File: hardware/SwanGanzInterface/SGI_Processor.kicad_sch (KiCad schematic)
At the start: 15 parts, among them J5 Conn_01x08_Pin, U7 LP-MSPM0G3507, U8 Adafruit ST7735R, U9 FT232R

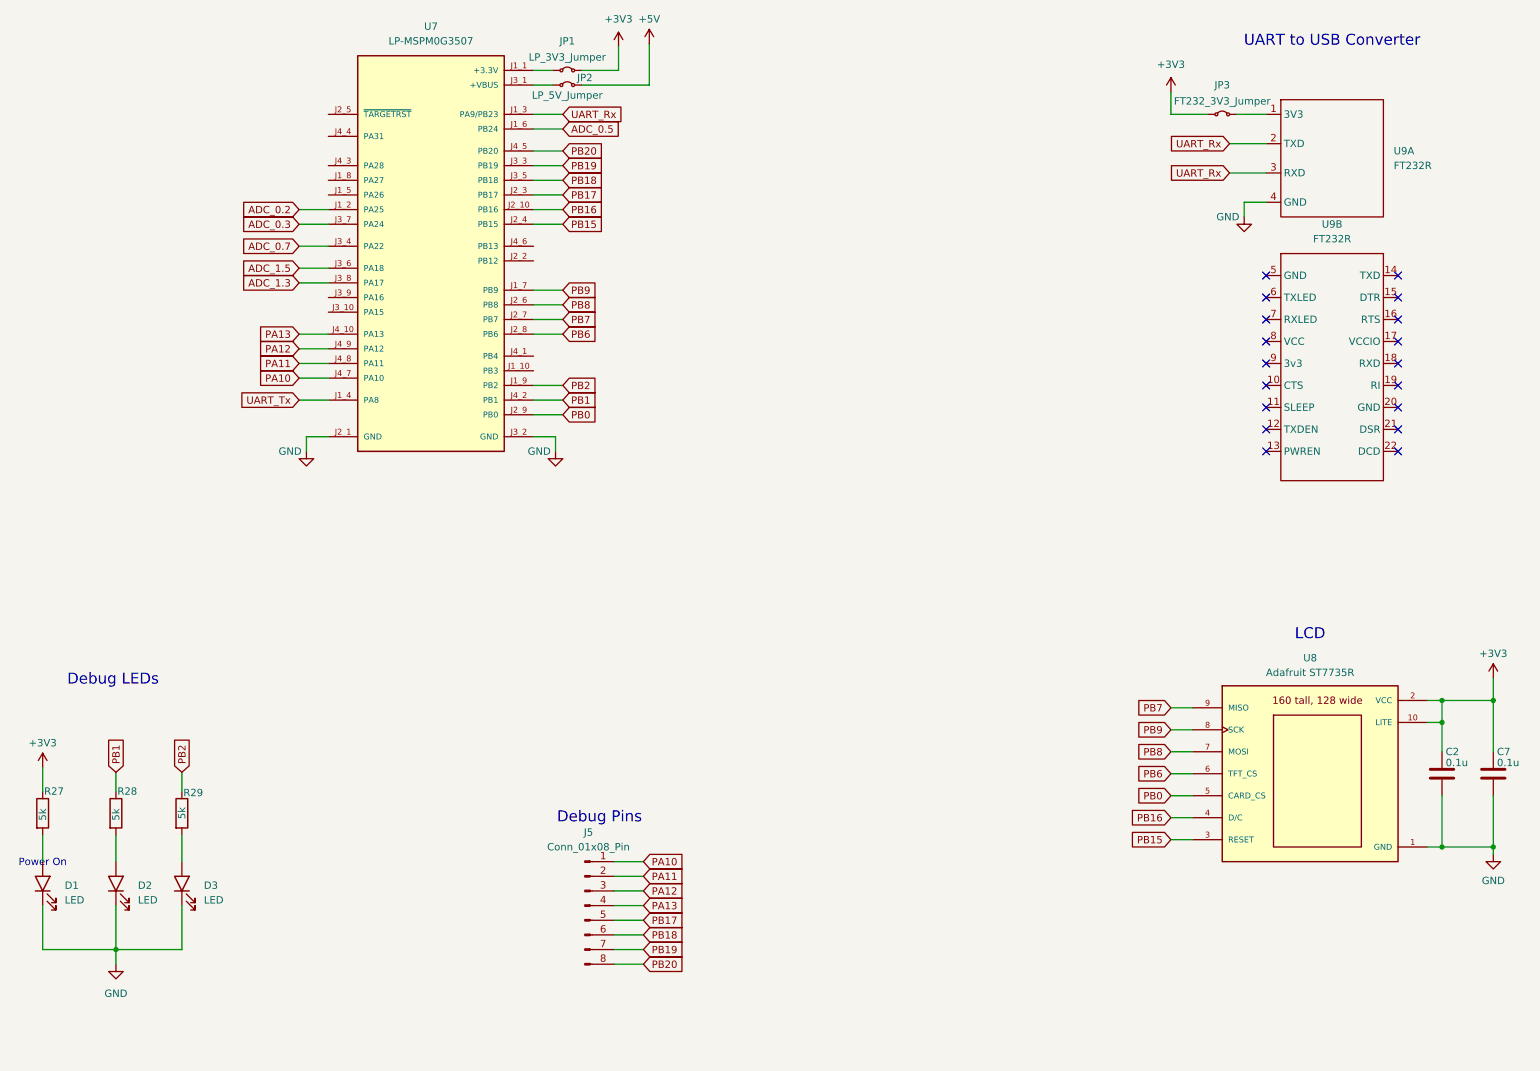
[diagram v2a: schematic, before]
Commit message: Added Test Points to the Outputs of Analog Circuits
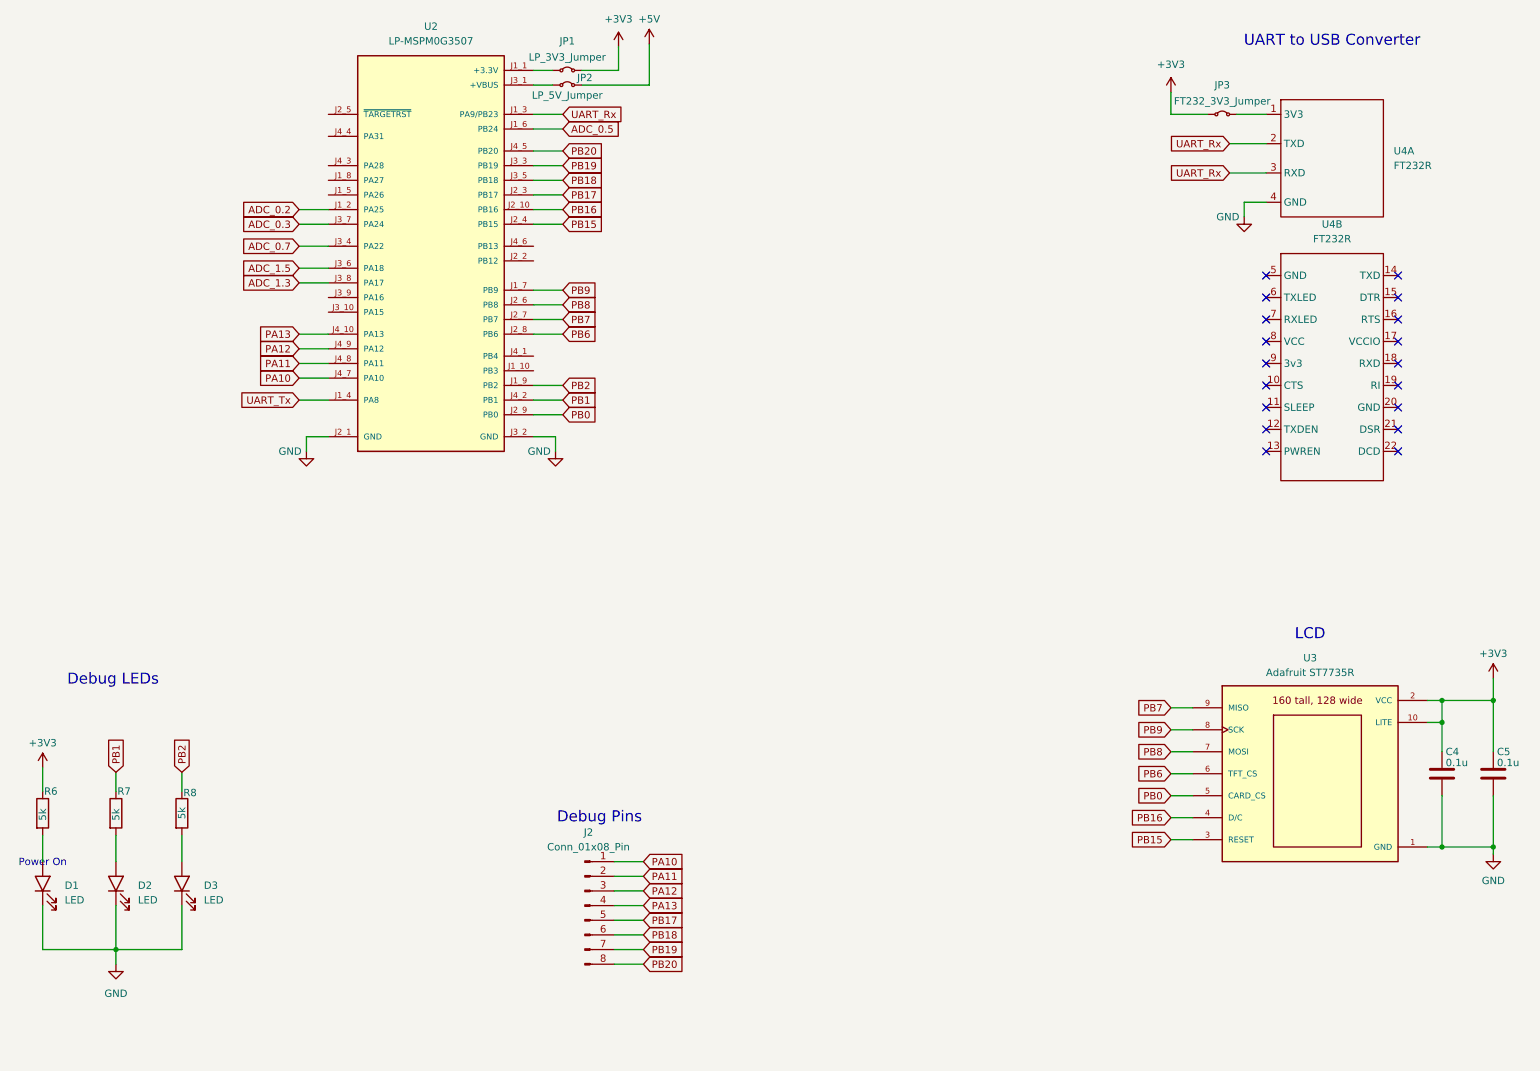
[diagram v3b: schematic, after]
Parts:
- C4: renamed from C2; footprint (none) -> Capacitor_SMD:C_0603_1608Metric
- C5: renamed from C7; footprint (none) -> Capacitor_SMD:C_0603_1608Metric
- renumbered J5 to J2, R27 to R6, R28 to R7, R29 to R8, U7 to U2, U8 to U3, U9 to U4
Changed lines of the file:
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@@
 		(on_board yes)
 		(dnp no)
-		(property "Reference" "#PWR058"
+		(property "Reference" "#PWR023"
 			(at 116.84 96.52 0)
 			(effects
@@
 			(project "SwanGanzInterface"
 				(path "/4e9a6e30-f660-472b-9696-bea1f34b4545/b7986f9d-7bcd-462e-9f66-fb6deb5be406"
-					(reference "#PWR058")
+					(reference "#PWR023")
 					(unit 1)
 				)
@@
 		(on_board yes)
 		(dnp no)
-		(property "Reference" "R27"
+		(property "Reference" "R6"
 			(at 28.194 149.098 0)
 			(effects
@@
 			(project ""
 				(path "/4e9a6e30-f660-472b-9696-bea1f34b4545/b7986f9d-7bcd-462e-9f66-fb6deb5be406"
-					(reference "R27")
+					(reference "R6")
 					(unit 1)
 				)
@@
 		(on_board yes)
 		(dnp no)
-		(property "Reference" "#PWR057"
+		(property "Reference" "#PWR022"
 			(at 73.66 96.52 0)
 			(effects
@@
 			(project "SwanGanzInterface"
 				(path "/4e9a6e30-f660-472b-9696-bea1f34b4545/b7986f9d-7bcd-462e-9f66-fb6deb5be406"
-					(reference "#PWR057")
+					(reference "#PWR022")
 					(unit 1)
 				)
@@
 		(dnp no)
 		(fields_autoplaced yes)
-		(property "Reference" "#PWR045"
+		(property "Reference" "#PWR029"
 			(at 279.4 166.37 0)
 			(effects
@@
 			(project ""
 				(path "/4e9a6e30-f660-472b-9696-bea1f34b4545/b7986f9d-7bcd-462e-9f66-fb6deb5be406"
-					(reference "#PWR045")
+					(reference "#PWR029")
 					(unit 1)
 				)
@@
 		(dnp no)
 		(fields_autoplaced yes)
-		(property "Reference" "J5"
+		(property "Reference" "J2"
 			(at 122.555 156.21 0)
 			(effects
@@
 			(project ""
 				(path "/4e9a6e30-f660-472b-9696-bea1f34b4545/b7986f9d-7bcd-462e-9f66-fb6deb5be406"
-					(reference "J5")
+					(reference "J2")
 					(unit 1)
 				)
@@
 		(dnp no)
 		(fields_autoplaced yes)
-		(property "Reference" "U9"
+		(property "Reference" "U4"
 			(at 251.46 50.8 0)
 			(effects
@@
 			(project ""
 				(path "/4e9a6e30-f660-472b-9696-bea1f34b4545/b7986f9d-7bcd-462e-9f66-fb6deb5be406"
-					(reference "U9")
+					(reference "U4")
 					(unit 2)
 				)
@@
 		(dnp no)
 		(fields_autoplaced yes)
-		(property "Reference" "#PWR049"
+		(property "Reference" "#PWR028"
 			(at 279.4 133.35 0)
 			(effects
@@
 			(project ""
 				(path "/4e9a6e30-f660-472b-9696-bea1f34b4545/b7986f9d-7bcd-462e-9f66-fb6deb5be406"
-					(reference "#PWR049")
+					(reference "#PWR028")
 					(unit 1)
 				)
@@
 		(dnp no)
 		(fields_autoplaced yes)
-		(property "Reference" "#PWR060"
+		(property "Reference" "#PWR025"
 			(at 133.096 23.368 0)
 			(effects
@@
 			(project ""
 				(path "/4e9a6e30-f660-472b-9696-bea1f34b4545/b7986f9d-7bcd-462e-9f66-fb6deb5be406"
-					(reference "#PWR060")
+					(reference "#PWR025")
 					(unit 1)
 				)
@@
 		(on_board yes)
 		(dnp no)
-		(property "Reference" "R29"
+		(property "Reference" "R8"
 			(at 52.324 149.352 0)
 			(effects
@@
 			(project "SwanGanzInterface"
 				(path "/4e9a6e30-f660-472b-9696-bea1f34b4545/b7986f9d-7bcd-462e-9f66-fb6deb5be406"
-					(reference "R29")
+					(reference "R8")
 					(unit 1)
 				)
@@
 		(dnp no)
 		(fields_autoplaced yes)
-		(property "Reference" "U9"
+		(property "Reference" "U4"
 			(at 262.128 38.0999 0)
 			(effects
@@
 			(project ""
 				(path "/4e9a6e30-f660-472b-9696-bea1f34b4545/b7986f9d-7bcd-462e-9f66-fb6deb5be406"
-					(reference "U9")
+					(reference "U4")
 					(unit 1)
 				)
@@
 		(dnp no)
 		(fields_autoplaced yes)
-		(property "Reference" "U8"
+		(property "Reference" "U3"
 			(at 247.65 125.984 0)
 			(effects
@@
 			(project ""
 				(path "/4e9a6e30-f660-472b-9696-bea1f34b4545/b7986f9d-7bcd-462e-9f66-fb6deb5be406"
-					(reference "U8")
+					(reference "U3")
 					(unit 1)
 				)
@@
 		(on_board yes)
 		(dnp no)
-		(property "Reference" "C7"
+		(property "Reference" "C5"
 			(at 280.035 142.24 0)
 			(effects
@@
 			)
 		)
-		(property "Footprint" ""
+		(property "Footprint" "Capacitor_SMD:C_0603_1608Metric"
 			(at 280.3652 149.86 0)
 			(effects
@@
 			(project "SwanGanzInterface"
 				(path "/4e9a6e30-f660-472b-9696-bea1f34b4545/b7986f9d-7bcd-462e-9f66-fb6deb5be406"
-					(reference "C7")
+					(reference "C5")
 					(unit 1)
 				)
@@
 		(dnp no)
 		(fields_autoplaced yes)
-		(property "Reference" "U7"
+		(property "Reference" "U2"
 			(at 95.25 16.51 0)
 			(effects
@@
 			(project ""
 				(path "/4e9a6e30-f660-472b-9696-bea1f34b4545/b7986f9d-7bcd-462e-9f66-fb6deb5be406"
-					(reference "U7")
+					(reference "U2")
 					(unit 1)
 				)
@@
 		(dnp no)
 		(fields_autoplaced yes)
-		(property "Reference" "#PWR061"
+		(property "Reference" "#PWR026"
 			(at 223.52 31.75 0)
 			(effects
@@
 			(project "SwanGanzInterface"
 				(path "/4e9a6e30-f660-472b-9696-bea1f34b4545/b7986f9d-7bcd-462e-9f66-fb6deb5be406"
-					(reference "#PWR061")
+					(reference "#PWR026")
 					(unit 1)
 				)
@@
 		(on_board yes)
 		(dnp no)
-		(property "Reference" "C2"
+		(property "Reference" "C4"
 			(at 271.145 142.24 0)
 			(effects
@@
 			)
 		)
-		(property "Footprint" ""
+		(property "Footprint" "Capacitor_SMD:C_0603_1608Metric"
 			(at 271.4752 149.86 0)
 			(effects
@@
 			(project "SwanGanzInterface"
 				(path "/4e9a6e30-f660-472b-9696-bea1f34b4545/b7986f9d-7bcd-462e-9f66-fb6deb5be406"
-					(reference "C2")
+					(reference "C4")
 					(unit 1)
 				)
@@
 		(on_board yes)
 		(dnp no)
-		(property "Reference" "#PWR062"
+		(property "Reference" "#PWR027"
 			(at 236.22 55.88 0)
 			(effects
@@
 			(project "SwanGanzInterface"
 				(path "/4e9a6e30-f660-472b-9696-bea1f34b4545/b7986f9d-7bcd-462e-9f66-fb6deb5be406"
-					(reference "#PWR062")
+					(reference "#PWR027")
 					(unit 1)
 				)
@@
 		(dnp no)
 		(fields_autoplaced yes)
-		(property "Reference" "#PWR051"
+		(property "Reference" "#PWR020"
 			(at 27.94 148.844 0)
 			(effects
@@
 			(project ""
 				(path "/4e9a6e30-f660-472b-9696-bea1f34b4545/b7986f9d-7bcd-462e-9f66-fb6deb5be406"
-					(reference "#PWR051")
+					(reference "#PWR020")
 					(unit 1)
 				)
@@
 		(dnp no)
 		(fields_autoplaced yes)
-		(property "Reference" "#PWR059"
+		(property "Reference" "#PWR024"
 			(at 127.762 23.876 0)
 			(effects
@@
 			(project ""
 				(path "/4e9a6e30-f660-472b-9696-bea1f34b4545/b7986f9d-7bcd-462e-9f66-fb6deb5be406"
-					(reference "#PWR059")
+					(reference "#PWR024")
 					(unit 1)
 				)
@@
 		(on_board yes)
 		(dnp no)
-		(property "Reference" "R28"
+		(property "Reference" "R7"
 			(at 40.894 149.098 0)
 			(effects
@@
 			(project "SwanGanzInterface"
 				(path "/4e9a6e30-f660-472b-9696-bea1f34b4545/b7986f9d-7bcd-462e-9f66-fb6deb5be406"
-					(reference "R28")
+					(reference "R7")
 					(unit 1)
 				)
@@
 		(dnp no)
 		(fields_autoplaced yes)
-		(property "Reference" "#PWR052"
+		(property "Reference" "#PWR021"
 			(at 40.64 185.42 0)
 			(effects
@@
 			(project ""
 				(path "/4e9a6e30-f660-472b-9696-bea1f34b4545/b7986f9d-7bcd-462e-9f66-fb6deb5be406"
-					(reference "#PWR052")
-					(unit 1)
-				)
+					(reference "#PWR021")
+					(unit 1)
+				)

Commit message: Footprints for most parts, added LCD Driver
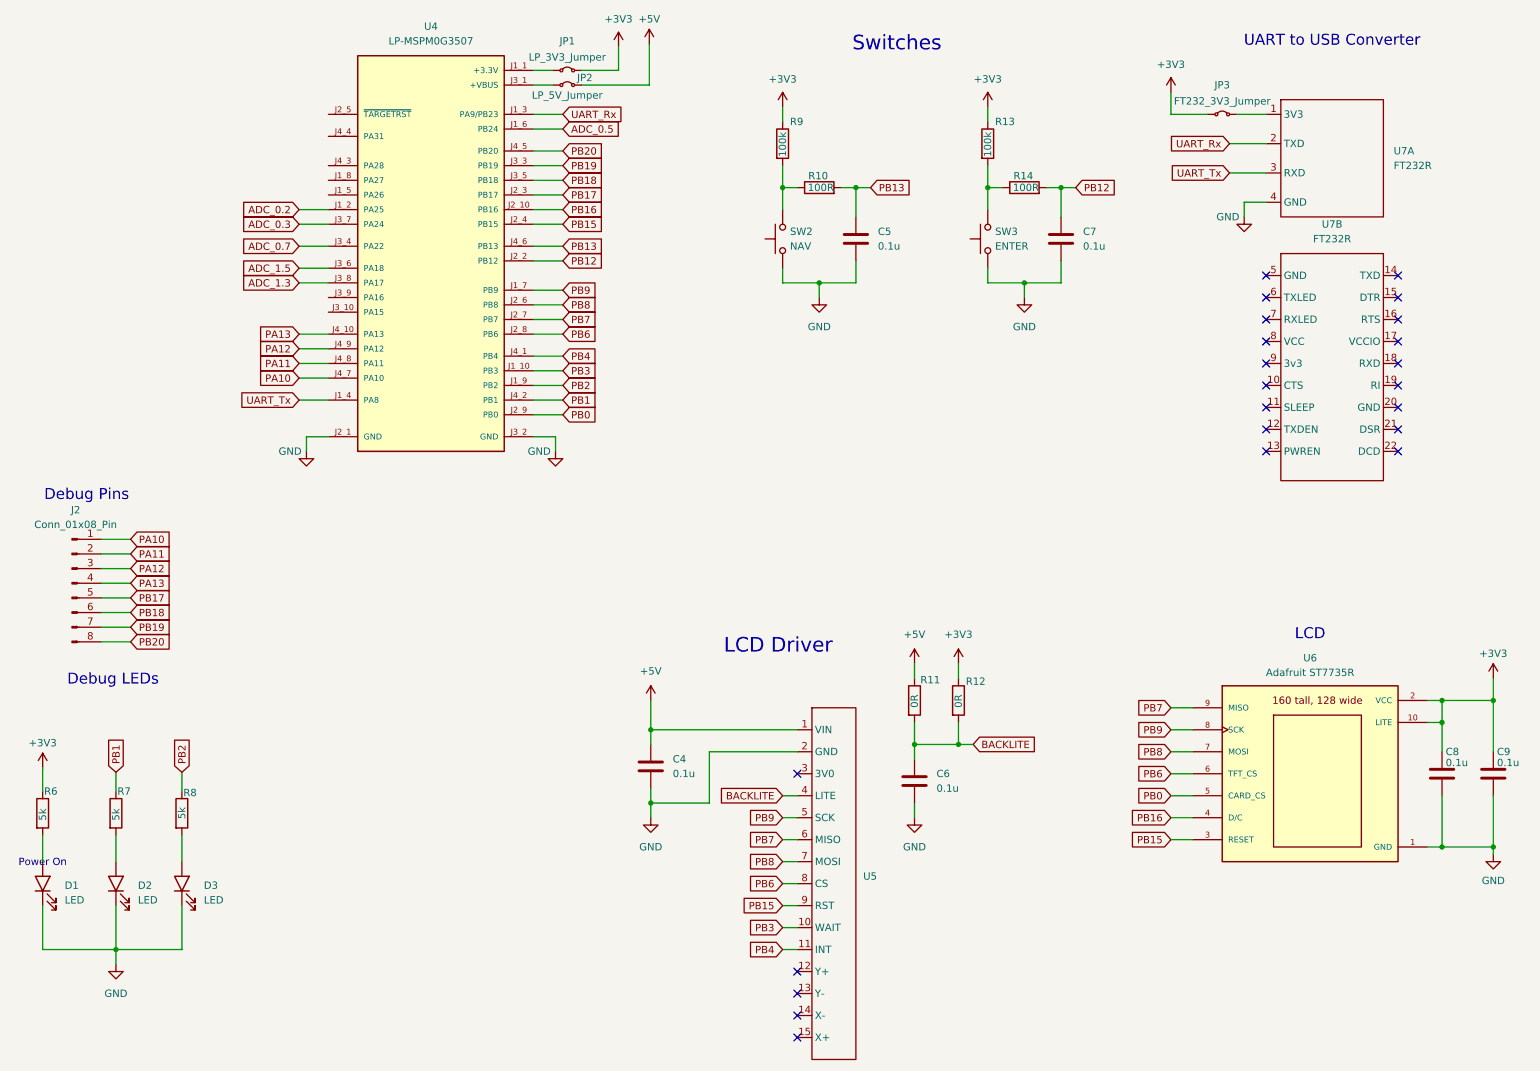
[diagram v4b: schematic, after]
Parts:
- added C4, C5, C6, C7: 0.1u, Capacitor_SMD:C_0603_1608Metric, symbol Device:C
- added R10, R14: 100R, Resistor_SMD:R_0603_1608Metric, symbol Device:R
- added R11, R12: 0R, Resistor_SMD:R_0603_1608Metric, symbol Device:R
- added R13, R9: 100k, Resistor_SMD:R_0603_1608Metric, symbol Device:R
- added SW2: NAV, SGI_FootprintsLib:SW_PUSH_6mm, symbol SGI_SymbolLib:SW_Push
- added SW3: ENTER, SGI_FootprintsLib:SW_PUSH_6mm, symbol SGI_SymbolLib:SW_Push
- added U5: ~, symbol SGI_SymbolLib:ADAFRUIT_1590_RA8875
- J2: footprint (none) -> Connector_PinHeader_2.54mm:PinHeader_1x08_P2.54mm_Vertical
- R6, R7, R8: footprint (none) -> Resistor_SMD:R_0603_1608Metric
- renumbered C4 to C8, C5 to C9, U2 to U4, U3 to U6, U4 to U7
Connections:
- net +3V3: now also R12.1, R13.1, R9.1
- net +5V: now also C4.1, R11.1, U5.1 (VIN)
- net GND: now also C4.2, C5.2, C6.2, C7.2, SW2.1, SW3.1, U5.2 (GND)
- net PB15: now also U5.9 (RST)
- net PB6: now also U5.8 (CS)
- net PB7: now also U5.6 (MISO)
- net PB8: now also U5.7 (MOSI)
- net PB9: now also U5.5 (SCK)
- net UART_Rx: no longer U7.3 (RXD)
- net UART_Tx: now also U7.3 (RXD)
- net PB3: now reaches U4.J1_10 (PB3)
- net PB3: now also U5.10 (WAIT)
- net PB12: now reaches U4.J2_2 (PB12)
- net PB12: now also C7.1, R14.2
- net PB4: now reaches U4.J4_1 (PB4)
- net PB4: now also U5.11 (INT)
- net PB13: now reaches U4.J4_6 (PB13)
- net PB13: now also C5.1, R10.2
- new net: R13.2, R14.1, SW3.2
- new net: R10.1, R9.2, SW2.2
- new net BACKLITE: C6.1, R11.2, R12.2, U5.4 (LITE)
- no-connect marks 18 -> 23
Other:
- note added: "LCD Driver"
- note added: "Switches"
- moved on the sheet: J2

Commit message: Started Layout
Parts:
- U5: value ~ -> AdaFruit_1590; footprint (none) -> SGI_FootprintsLib:AdaFruit_1590
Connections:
- net GND: now also D1.1 (K), D2.1 (K), D3.1 (K)
- no-connect marks 23 -> 30
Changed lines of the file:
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@@
 	)
 	(no_connect
+		(at 77.47 43.18)
+	)
+	(no_connect
+		(at 77.47 63.5)
+	)
+	(no_connect
 		(at 158.75 146.05)
 	)
@@
 	)
 	(no_connect
+		(at 77.47 45.72)
+	)
+	(no_connect
 		(at 262.89 78.74)
 	)
@@
 	)
 	(no_connect
+		(at 77.47 40.64)
+	)
+	(no_connect
 		(at 240.03 63.5)
 	)
@@
 	)
 	(no_connect
+		(at 77.47 31.75)
+	)
+	(no_connect
 		(at 240.03 67.31)
 	)
@@
 	)
 	(no_connect
+		(at 77.47 35.56)
+	)
+	(no_connect
 		(at 240.03 74.93)
 	)
@@
 	)
 	(no_connect
+		(at 77.47 66.04)
+	)
+	(no_connect
 		(at 262.89 59.69)
 	)
@@
 	(wire
 		(pts
-			(xy 40.64 176.784) (xy 40.64 179.07)
+			(xy 40.64 176.53) (xy 40.64 179.07)
 		)
 		(stroke
@@
 		(on_board yes)
 		(dnp no)
-		(fields_autoplaced yes)
 		(property "Reference" "U5"
-			(at 170.18 163.8299 0)
+			(at 169.545 160.655 0)
 			(effects
 				(font
@@
 			)
 		)
-		(property "Value" "~"
-			(at 170.18 166.3699 0)
+		(property "Value" "AdaFruit_1590"
+			(at 169.545 162.56 0)
 			(effects
 				(font
@@
 			)
 		)
-		(property "Footprint" ""
+		(property "Footprint" "SGI_FootprintsLib:AdaFruit_1590"
 			(at 168.91 165.1 0)
 			(effects

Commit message: Started Routing
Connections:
- net PB18: no longer J2.6 (Pin_6)
- net PB19: no longer J2.7 (Pin_7)
- net PA28: now reaches U4.J4_3 (PA28)
- net PA28: now also J2.6 (Pin_6)
- net PA31: now reaches U4.J4_4 (PA31)
- net PA31: now also J2.7 (Pin_7)
- no-connect marks 30 -> 28

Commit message: Valvano Changes
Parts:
- D1: value LED -> +3V3
- D2: value LED -> WORKING
- D3: value LED -> ERROR
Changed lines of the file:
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@@
 		(on_board yes)
 		(dnp no)
-		(fields_autoplaced yes)
 		(property "Reference" "D2"
 			(at 44.45 165.4174 0)
@@
 			)
 		)
-		(property "Value" "LED"
+		(property "Value" "WORKING"
 			(at 44.45 167.9574 0)
 			(effects
@@
 			)
 		)
-		(property "Value" "LED"
+		(property "Value" "ERROR"
 			(at 55.88 167.9574 0)
 			(effects
@@
 			)
 		)
-		(property "Value" "LED"
+		(property "Value" "+3V3"
 			(at 31.75 167.9574 0)
 			(effects
